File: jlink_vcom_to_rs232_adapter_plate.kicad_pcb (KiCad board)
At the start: 2 copper layers, 60 x 38 mm, 15 parts, among them J1 Conn_02x10_Odd_Even, J2 Conn_01x04, J3 Conn_02x10_Odd_Even, J4 Conn_01x06, J5 DB9_Male, J6 Conn_01x03, J7 Conn_01x03, U1 MAX232

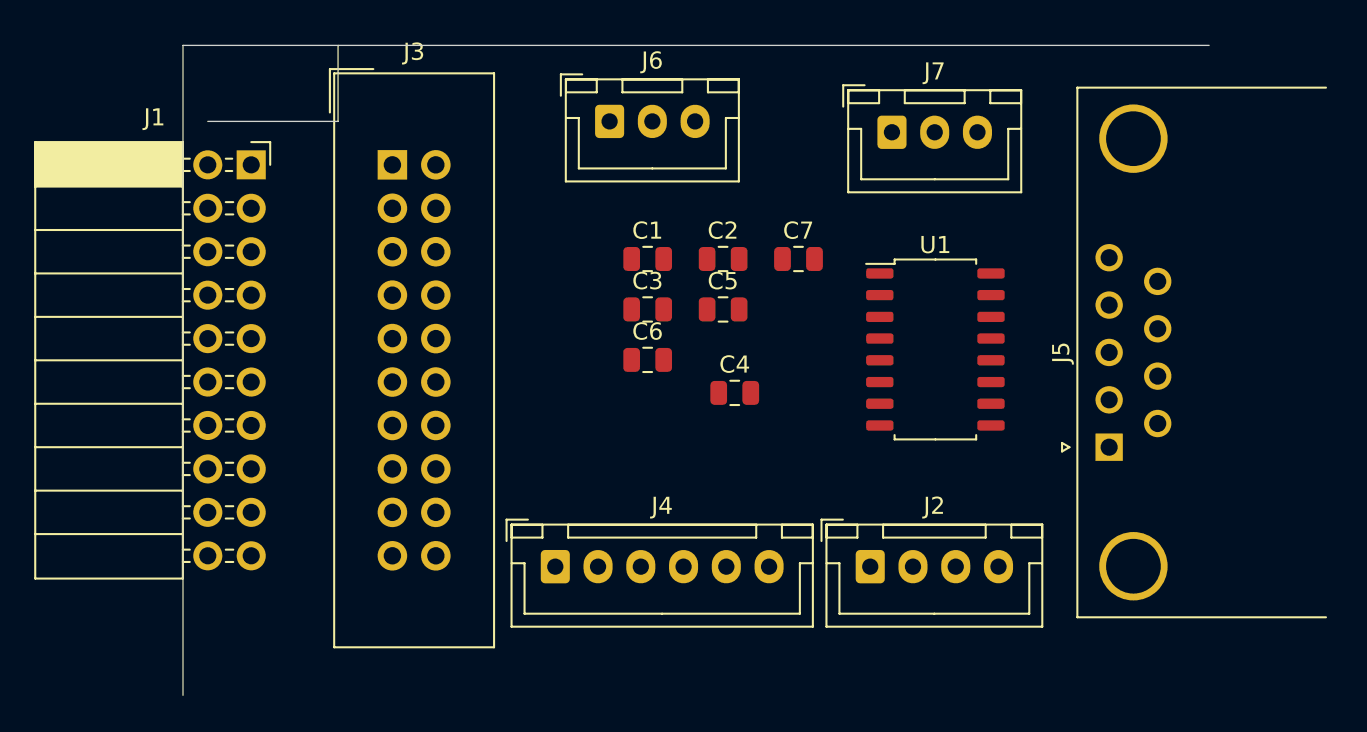
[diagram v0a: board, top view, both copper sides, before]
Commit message: 1、增加 H7_TOOL 专用 SWD 接口 2、增加 XH-5A 接口
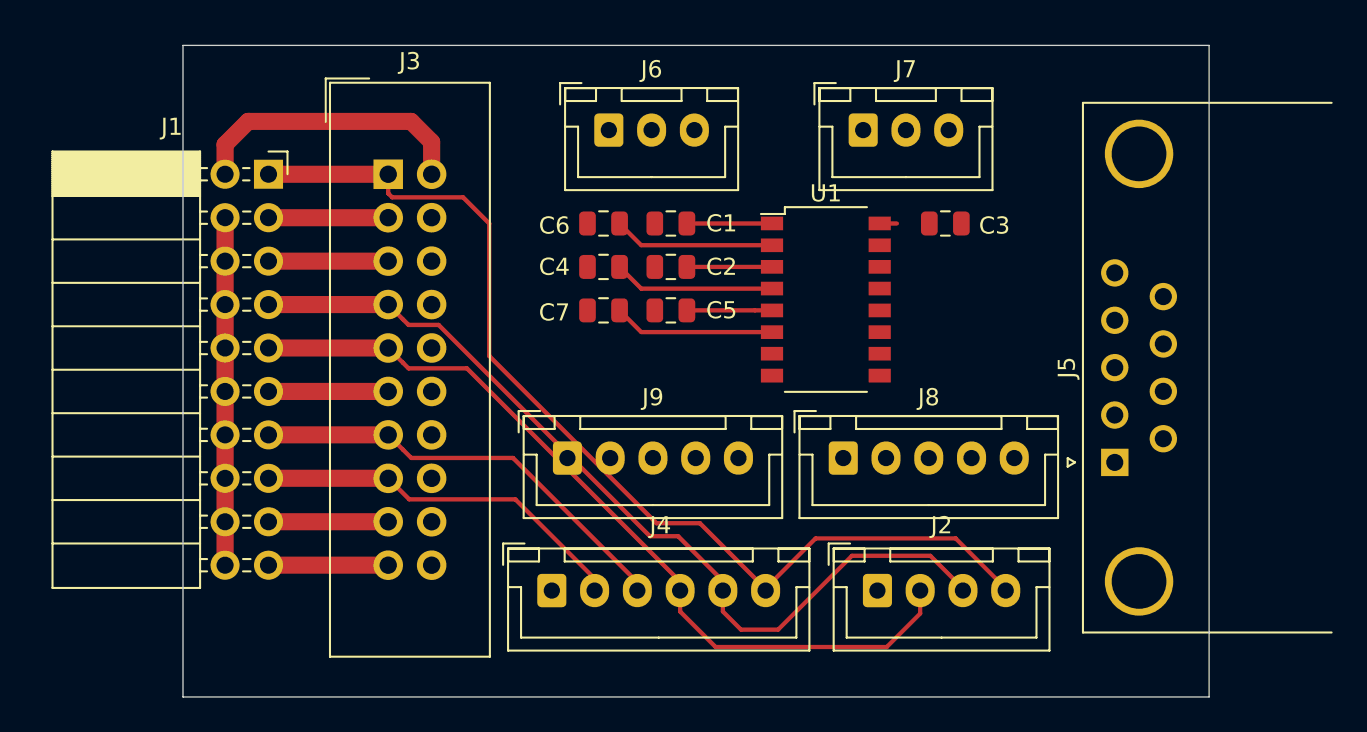
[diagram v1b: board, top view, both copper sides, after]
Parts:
- added J8: h7_tool_swd, Connector_JST:JST_XH_B5B-XH-A_1x05_P2.50mm_Vertical, F.Cu at (208.6, 61.6)
- added J9: Conn_01x05, Connector_JST:JST_XH_B5B-XH-A_1x05_P2.50mm_Vertical, F.Cu at (192.5, 61.6)
- U1: footprint Package_SO:SOP-16_4.55x10.3mm_P1.27mm -> Package_SO:SOP-16_4.4x10.4mm_P1.27mm
- moved C3 18.1 mm to (214.6, 47.9), turned to 180 degrees
- moved C7 11.8 mm to (194.6, 53.0)
- moved C4 10.6 mm to (194.6, 50.4)
- moved C6 8.38 mm to (194.6, 47.9)
- moved U1 7.04 mm to (207.6, 52.3)
- moved C2 3.09 mm to (198.5, 50.4), turned to 180 degrees
- moved C5 3.05 mm to (198.5, 53.0)
- moved C1 2.48 mm to (198.5, 47.9), turned to 180 degrees
- moved J7 1.69 mm to (209.8, 42.4)
- moved J2 1.46 mm to (210.6, 69.3)
- moved J4 1.41 mm to (191.6, 69.3)
- moved J1 1.15 mm to (175.0, 45.0)
- moved J5 0.95 mm to (224.5, 61.8)
- moved J3 0.60 mm to (182.0, 45.0)
- moved J6 0.51 mm to (194.9, 42.4)
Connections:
- C5 pad 2: (no net) -> Net-(C5-Pad2)
- J2 pad 1: /VTref -> GND
- J2 pad 2: /TMS -> /TCK
- J2 pad 3: /TCK -> /TMS
- J2 pad 4: GND -> /VTref
- J4 pad 1: /VTref -> GND
- J4 pad 2: /TMS -> /nRESET
- J4 pad 3: /TCK -> /TDO
- J4 pad 4: /TDO -> /TCK
- J4 pad 5: /nRESET -> /TMS
- J4 pad 6: GND -> /VTref
- U1 pad 5: (no net) -> Net-(C5-Pad2)
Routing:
- net /VTref: track 0.00 -> 61.1 mm
- net /TMS: track 0.00 -> 52.2 mm
- net /TCK: track 0.00 -> 48.5 mm
- net /TDO: track 0.00 -> 25.6 mm
- net /nRESET: track 0.00 -> 22.2 mm
- net GND: track 0.00 -> 20.3 mm
- net (no net): track 0.00 -> 16.8 mm
- net Net-(C6-Pad2): track 0.00 -> 9.34 mm
- net Net-(C4-Pad2): track 0.00 -> 9.34 mm
- net Net-(C7-Pad2): track 0.00 -> 9.34 mm
- net /5V-Supply: track 0.00 -> 7.90 mm
- net /nTRST: track 0.00 -> 7.00 mm
- net /RTCK: track 0.00 -> 7.00 mm
- net /JLINK_TXD: track 0.00 -> 7.00 mm
- net /DBGRQ: track 0.00 -> 7.00 mm
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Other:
- board size 60 x 38 mm -> 60 x 38.1 mm

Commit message: 1、增加 电源 LED 灯 指示 2、布线 完成 3、泪滴 增加完成 4、覆铜 完成
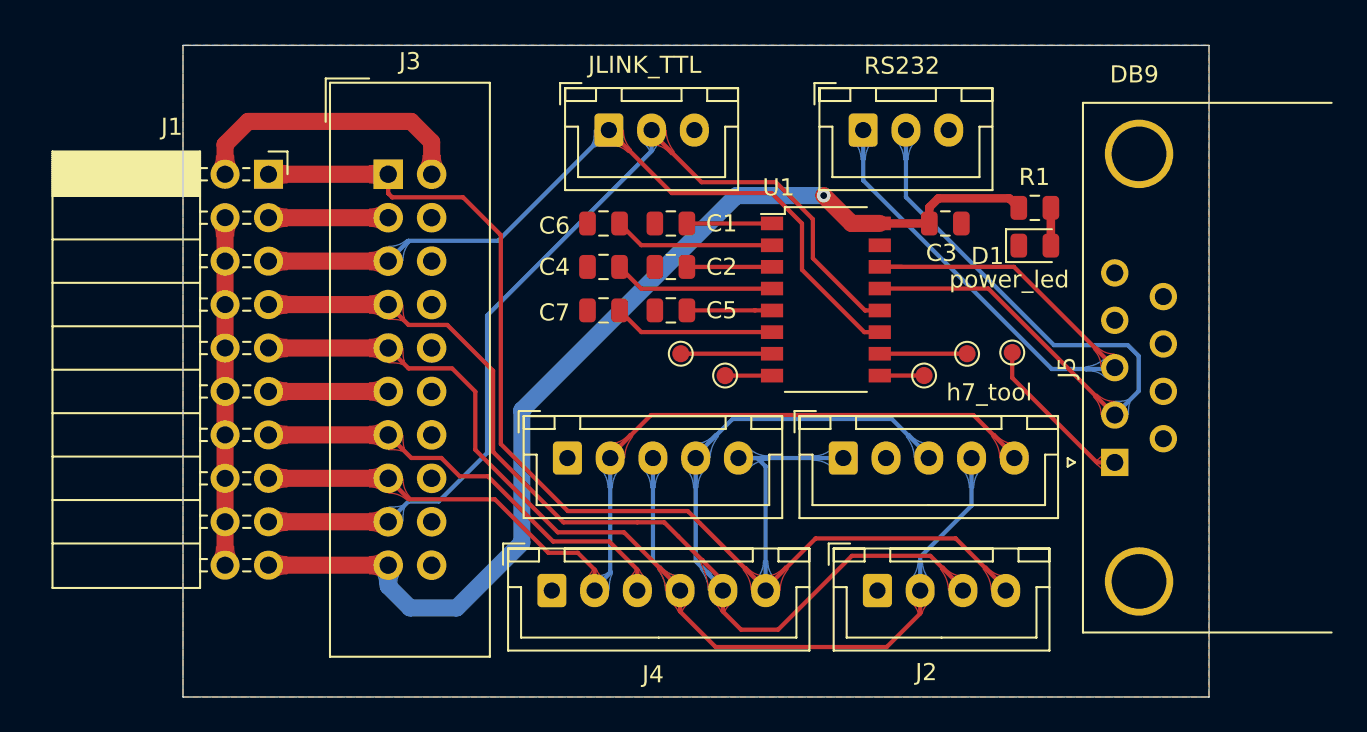
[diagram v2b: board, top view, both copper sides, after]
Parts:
- added D1: LED, LED_SMD:LED_0805_2012Metric, F.Cu at (219.8, 49.2)
- added R1: R, Resistor_SMD:R_0805_2012Metric, F.Cu at (219.8, 47.0)
- added REF**: KiCad-Logo_5mm_SilkScreen, Symbol:KiCad-Logo_5mm_SilkScreen, B.Cu at (200.5, 53.6)
- added TP1: TestPoint, TestPoint:TestPoint_Pad_D1.0mm, F.Cu at (215.8, 55.5)
- added TP2: TestPoint, TestPoint:TestPoint_Pad_D1.0mm, F.Cu at (213.3, 56.8)
- added TP3: TestPoint, TestPoint:TestPoint_Pad_D1.0mm, F.Cu at (218.5, 55.4)
- added TP4: TestPoint, TestPoint:TestPoint_Pad_D1.0mm, F.Cu at (199.1, 55.5)
- added TP5: TestPoint, TestPoint:TestPoint_Pad_D1.0mm, F.Cu at (201.7, 56.8)
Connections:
- J5 pad 1: (no net) -> Net-(J5-Pad1)
- U1 pad 10: (no net) -> Net-(TP1-Pad1)
- U1 pad 7: (no net) -> Net-(TP4-Pad1)
- U1 pad 8: (no net) -> Net-(TP5-Pad1)
- U1 pad 9: (no net) -> Net-(TP2-Pad1)
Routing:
- net /5V-Supply: track 7.90 -> 65.0 mm, vias 0 -> 1
- net /DBGRQ: track 7.00 -> 56.4 mm
- net /RS232_RXD: track 0.00 -> 42.3 mm
- net /RS232_TXD: track 0.00 -> 39.7 mm
- net /JLINK_TXD: track 7.00 -> 45.4 mm
- net /nRESET: track 22.2 -> 56.5 mm
- net /TMS: track 52.2 -> 79.1 mm
- net /TCK: track 48.5 -> 68.2 mm
- net /VTref: track 61.1 -> 78.9 mm
- net Net-(J5-Pad1): track 0.00 -> 9.52 mm
- net Net-(TP4-Pad1): track 0.00 -> 5.33 mm
- net Net-(TP1-Pad1): track 0.00 -> 5.11 mm
- net Net-(TP5-Pad1): track 0.00 -> 2.74 mm
- net Net-(TP2-Pad1): track 0.00 -> 2.59 mm
- net Net-(D1-Pad2): track 0.00 -> 2.21 mm
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- added copper zone on B.Cu, net GND
- added copper zone on F.Cu, net GND
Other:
- board text added: "2019-11-7 17:18:12"
- board text added: "5V"
- board text added: "CLK"
- board text added: "DB9"
- board text added: "DBGRQ"
- board text added: "DESIGN BY SUOZHANG"
- board text added: "DIO"
- board text added: "GND"
- board text added: "JLINK_TTL"
- board text added: "NC"
- board text added: "RS232"
- board text added: "RS232_GND"
- board text added: "RS232_RXD"
- board text added: "RS232_TXD"
- board text added: "RTCK"
- board text added: "RXD"
- board text added: "SWO"
- board text added: "TCK"
- board text added: "TDI"
- board text added: "TDO"
- board text added: "TMS"
- board text added: "TXD"
- board text added: "VTref"
- board text added: "h7_tool"
- board text added: "nRST"
- board text added: "nTRST"
- board text added: "power_led"

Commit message: 1、修改 每个 元器件 为实际的 value 2、生成了 geber 文件
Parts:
- removed REF**: KiCad-Logo_5mm_SilkScreen, Symbol:KiCad-Logo_5mm_SilkScreen
- C1, C2, C3, C4, C5, C6, C7: value CAP -> 220nF(224) ±10% 16V
- D1: value LED -> green
- J1: value Conn_02x10_Odd_Even -> 排母 2*10P 2.54mm 弯针
- J2: value Conn_01x04 -> XH-4A
- J3: value Conn_02x10_Odd_Even -> 2.54mm 2*10P 直 简牛
- J4: value Conn_01x06 -> XH-6A
- J5: value DB9_Male -> DMR-XP 公头叉锁 9P 半金
- J6, J7: value Conn_01x03 -> XH-3A
- J8: value h7_tool_swd -> XH-5A
- J9: value Conn_01x05 -> XH-5A
- R1: value R -> 10K
- U1: value MAX232 -> UT3232G-S16-R
